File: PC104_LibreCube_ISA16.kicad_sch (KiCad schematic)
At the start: 12 parts

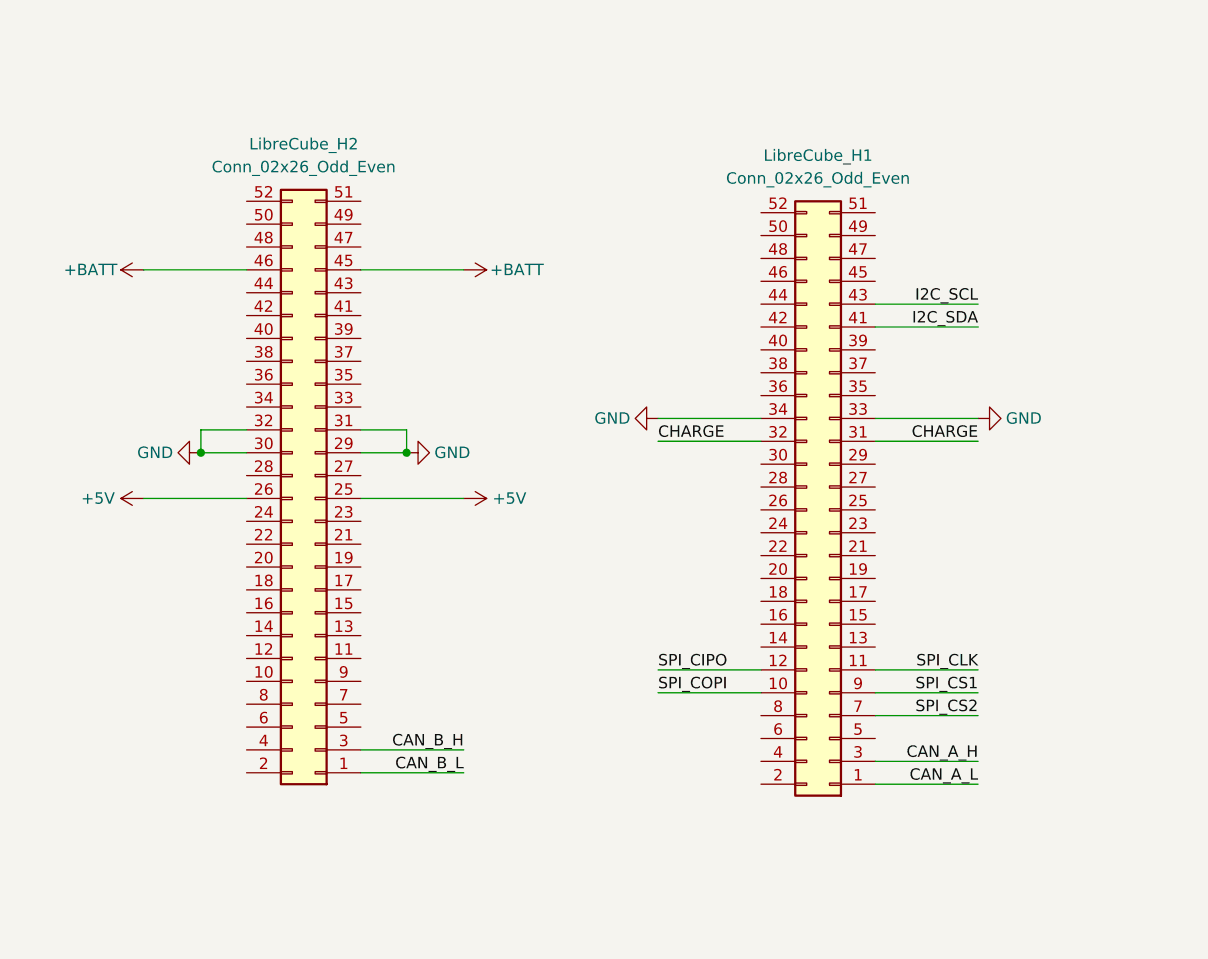
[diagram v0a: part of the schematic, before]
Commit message: Suppression de la connectique LibreCube
git-svn-id: file:///D%5C00%20-%20Dev%20&%20Calculs%5CRepoTortoiseSVN_PCB%5CPC104_Template/branches/PC104_ISA_16bits@13 5901225d-b6fc-0a46-af7b-916857fbd23b
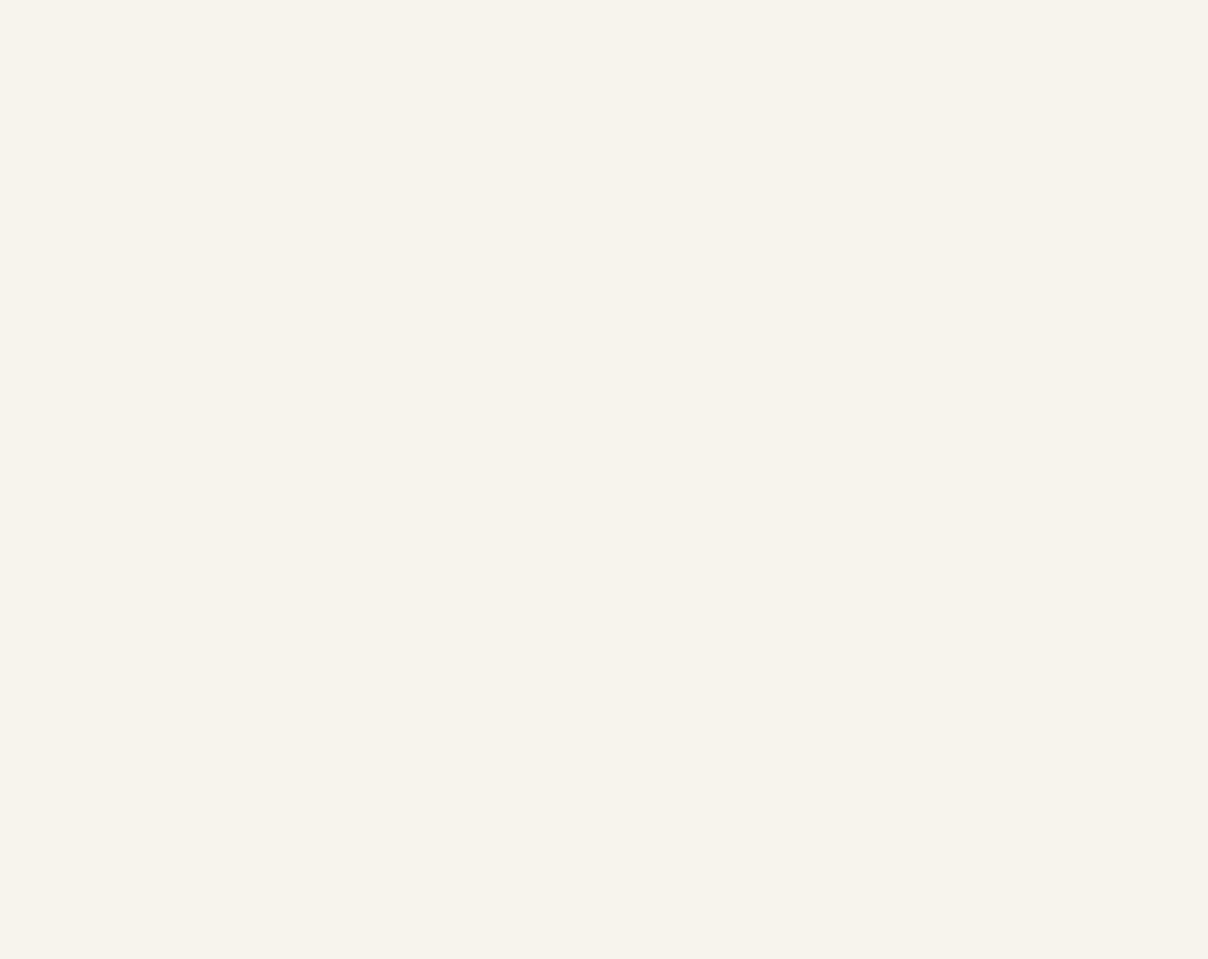
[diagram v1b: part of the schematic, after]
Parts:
- removed LibreCube_H1, LibreCube_H2: Conn_02x26_Odd_Even, Connector_PinHeader_2.54mm:PinHeader_2x26_P2.54mm_Vertical, symbol Connector_Generic:Conn_02x26_Odd_Even
